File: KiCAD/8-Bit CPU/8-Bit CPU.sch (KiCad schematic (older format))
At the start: 2 parts, among them SW1 SW_Push

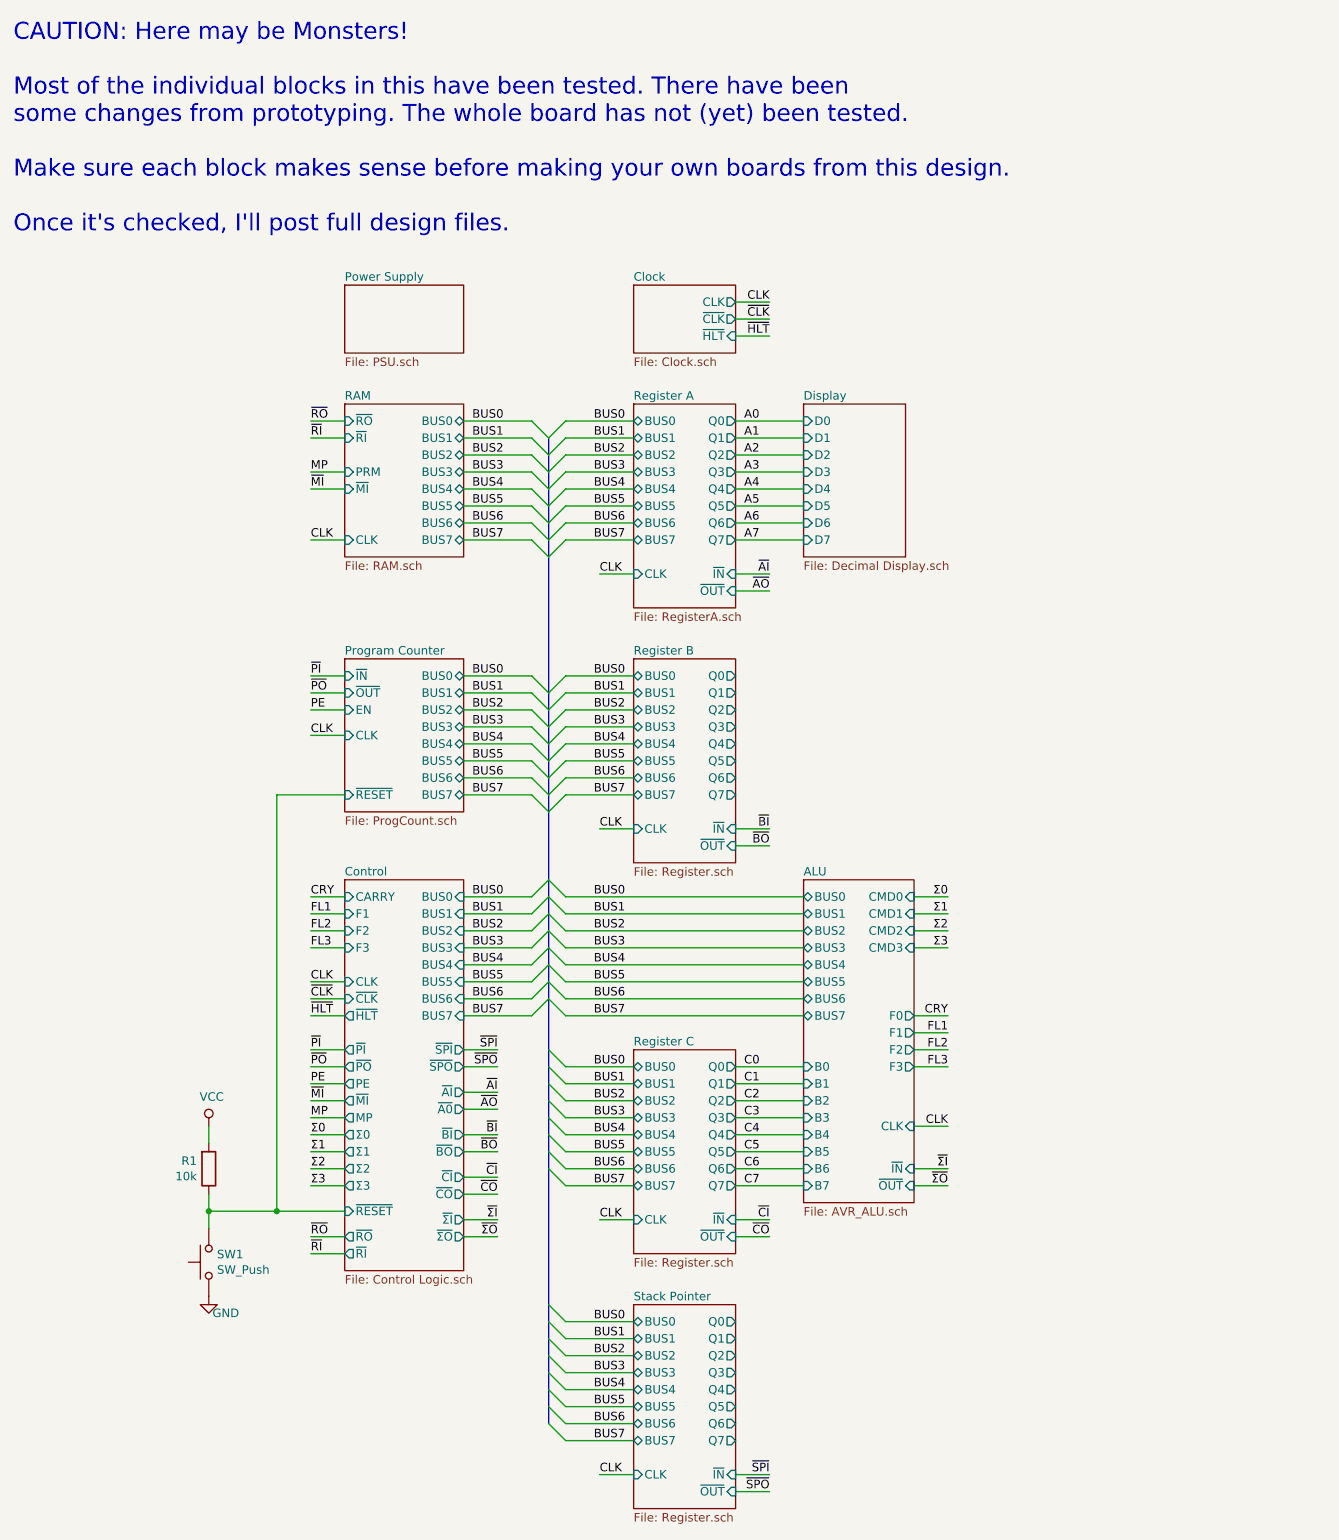
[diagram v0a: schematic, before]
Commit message: KiCAD cleanup - Revision A
Revision A Known Issues:
 * ATTiny45 has incorrect footprint
 * Flags register is redundant (The ATMega16's output port is a register)
 * Power jack pinout is wrong (12V shorted to ground)
 * Step counter reset logic is wrong (Active high signalling, Active low input)
 * ALU output indicator not connected
 * HLT indicator missing
 * EEPROMs can't be page written due to addressing setup (minor annoyance)
 * Flags Logic uses NAND gates instead of AND (fixed on the board I built)
 * Programmer needs to be able to toggle EEPROM outputs and Addressing Devices
    with different signals to enable reading.
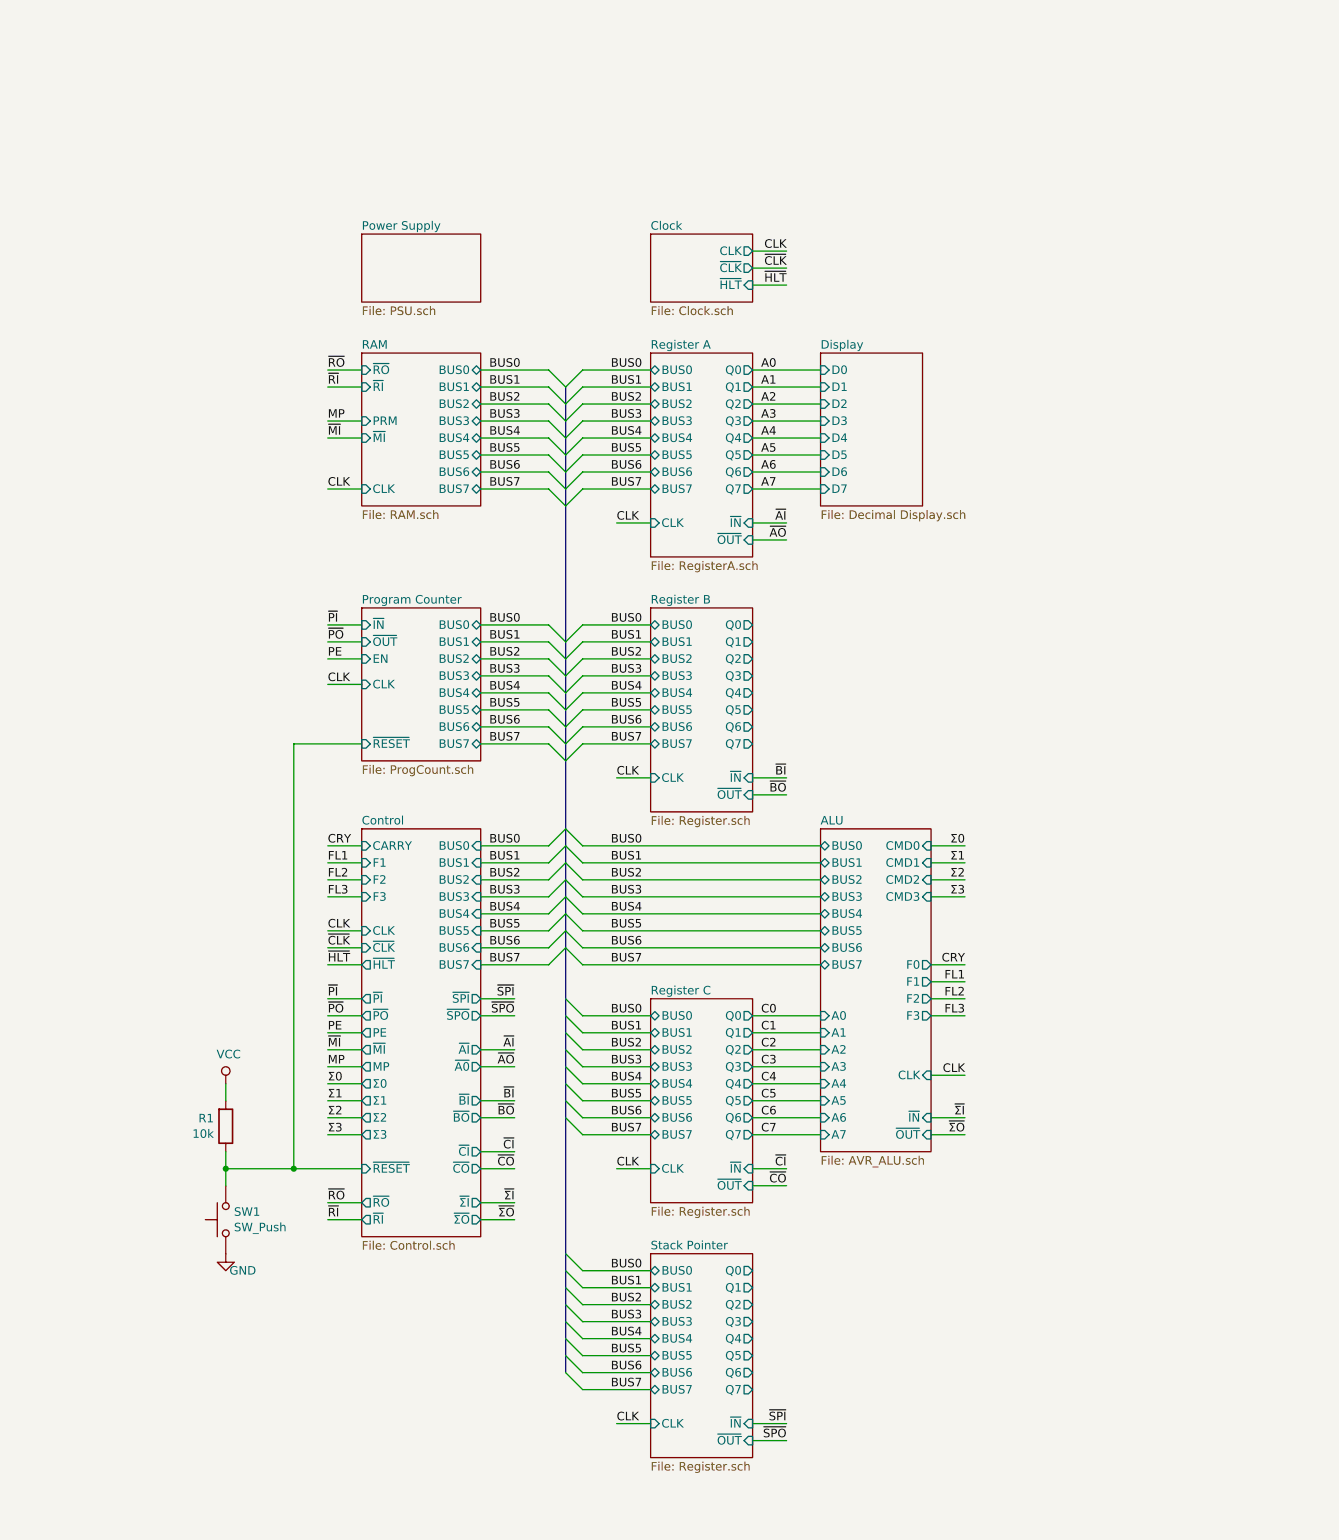
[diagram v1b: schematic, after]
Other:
- note removed: "CAUTION: Here may be Monsters!\n\nMost of the individual blocks in this have been tested. There have been\nsome changes from prototyping. The whole board has not (yet) been tested.\n\nMake sure each block makes sense before making your own boards from this design.\n\nOnce it's checked, I'll post full design files."
- moved on the sheet: R1, SW1

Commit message: KiCAD files update & Gerbers
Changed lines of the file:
@@
 encoding utf-8
 Sheet 1 29
-Title ""
+Title "8 Bit Computer"
 Date ""
-Rev ""
+Rev "C"
 Comp ""
 Comment1 ""
@@
 	2200 4800 2200 7300
 Text Label 6150 6400 2    50   ~ 0
-FL3
+OVF
 Text Label 6150 6300 2    50   ~ 0
-FL2
+NEG
 Text Label 6150 6200 2    50   ~ 0
-FL1
+ZER
 Text Label 6150 6100 2    50   ~ 0
 CRY
@@
 	2600 6800 2400 6800
 Text Label 2400 5700 0    50   ~ 0
-FL3
+OVF
 Text Label 2400 5600 0    50   ~ 0
-FL2
+NEG
 Text Label 2400 5500 0    50   ~ 0
-FL1
+ZER
 Wire Wire Line
 	2600 5700 2400 5700
